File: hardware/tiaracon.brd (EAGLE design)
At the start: 50 x 50 mm, 21 parts, among them U1 ATTINY45

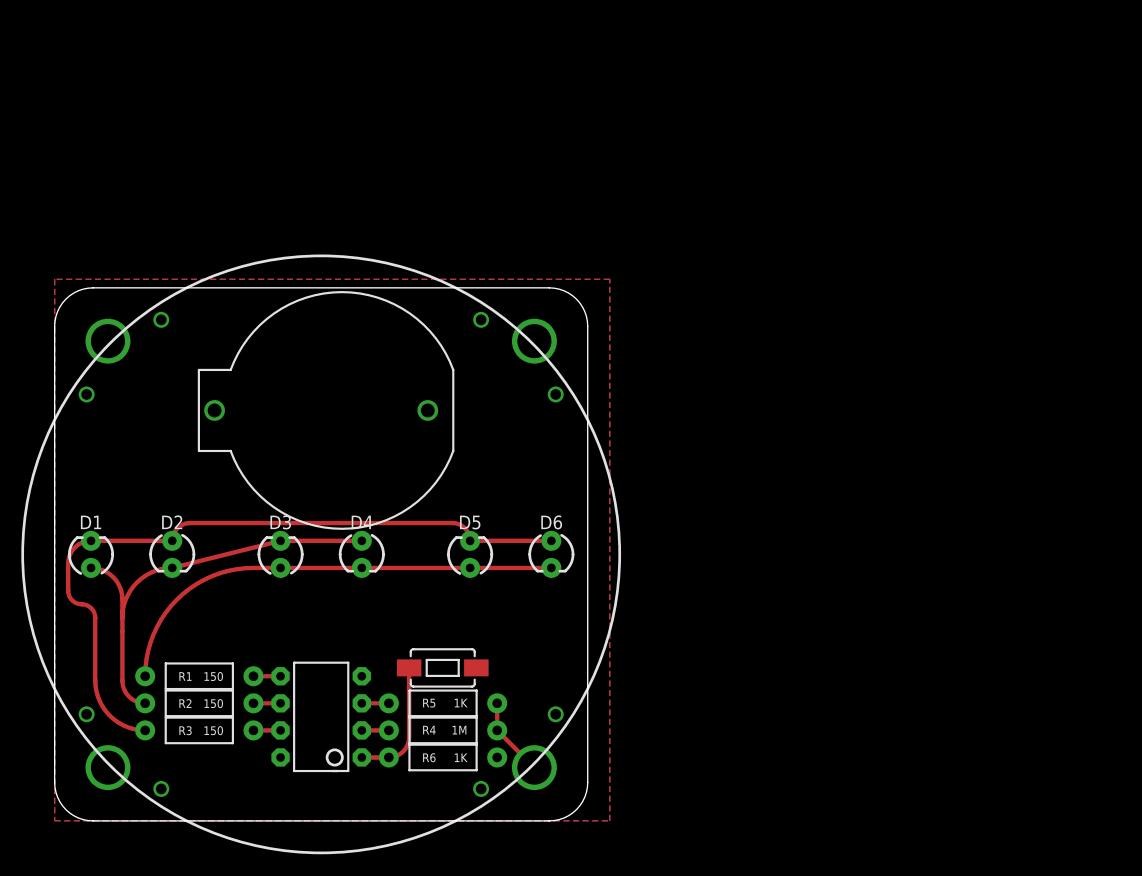
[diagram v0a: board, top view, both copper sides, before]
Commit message: adding tiara artwork, inital attempt at rough layout of components. No traces yet.
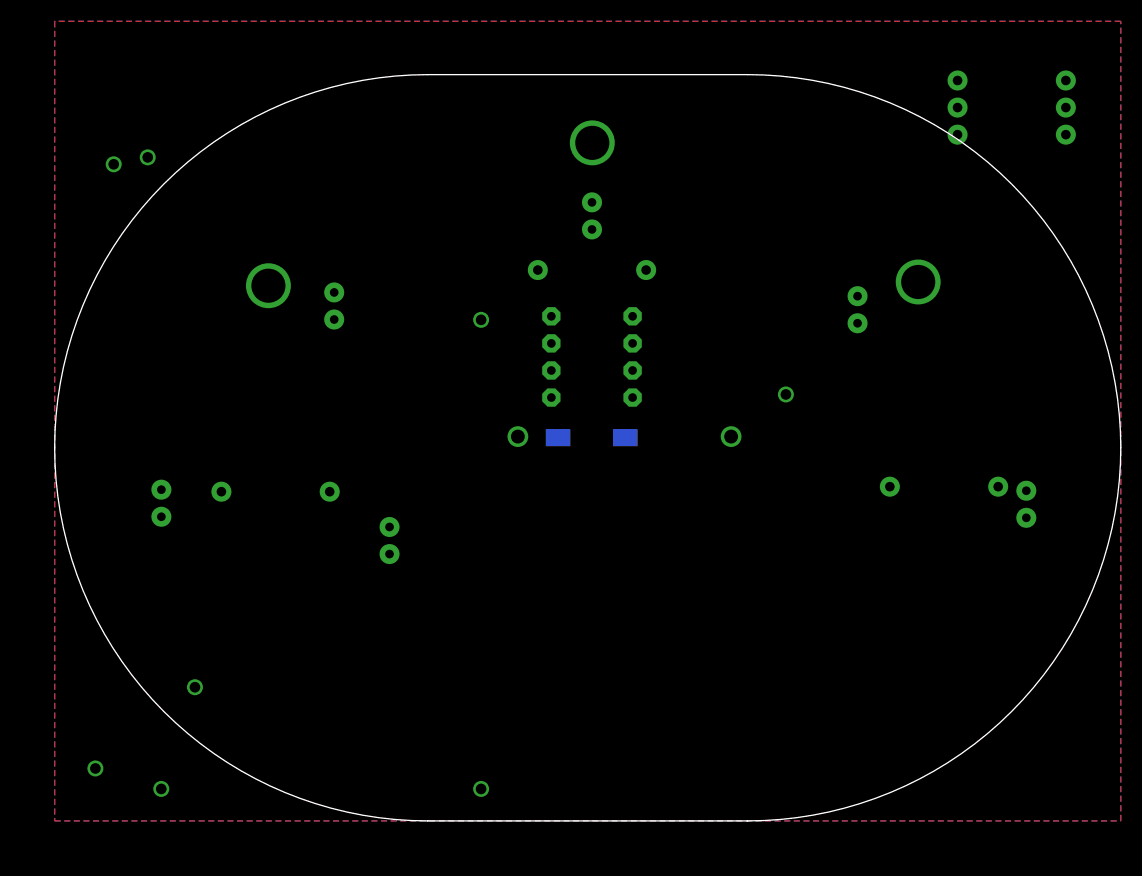
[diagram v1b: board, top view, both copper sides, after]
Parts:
- removed U$2, U$3, U$4, U$5, U$6: (no value), firefly:FIREFLY
- U$1: device securinghardware:SECURINGHARDWAREDOTCOM -> tiaracon:TIARA
- moved R4 79.1 mm to (89.8, 66.9), flipped to the bottom
- moved R5 79.1 mm to (89.8, 69.5), flipped to the bottom
- moved R6 79.1 mm to (89.8, 64.4), flipped to the bottom
- moved R2 72.7 mm to (83.4, 31.4), flipped to the bottom
- moved D4 62.5 mm to (91.1, 29.7), flipped to the bottom, turned to 90 degrees
- moved D3 58.8 mm to (75.3, 48.0), flipped to the bottom, turned to 270 degrees
- moved R3 56.8 mm to (50.4, 51.7), flipped to the bottom
- moved U$1 54.9 mm to (0.00, 0.00), flipped to the top
- moved U1 42.2 mm to (50.4, 43.5), flipped to the bottom
- moved D5 33.7 mm to (50.4, 56.8), flipped to the bottom
- moved D2 27.8 mm to (26.2, 48.3), flipped to the bottom, turned to 90 degrees
- moved S1 25.7 mm to (50.4, 35.9), flipped to the bottom
- moved BAT1 24.9 mm to (51.6, 36.0), flipped to the bottom
- moved R1 18.7 mm to (20.7, 30.9), flipped to the bottom, turned to 0 degrees
- moved D6 15.2 mm to (31.4, 26.3), flipped to the bottom, turned to 90 degrees
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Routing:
- net N$7: track 66.2 -> 0.00 mm
- net N$6: track 42.3 -> 0.00 mm
- net N$8: track 39.5 -> 0.00 mm
- net N$11: track 11.7 -> 0.00 mm
- net RING: track 7.48 -> 0.00 mm, vias 1 -> 0
- net N$5: track 2.54 -> 0.00 mm
- net N$4: track 2.54 -> 0.00 mm
- net N$3: track 2.54 -> 0.00 mm
- net N$2: track 2.54 -> 0.00 mm
- net N$1: track 2.54 -> 0.00 mm
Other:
- board size 50 x 50 mm -> 100 x 70 mm
- board text removed: "Jar of Fireflies"
- board text removed: "Jar of Fireflies V1.1 https://git.io/fireflies"
- board text removed: "Joe FitzPatrick @securelyfitz"
- board text removed: "by @securelyfitz"
- board text removed: "joefitz@securinghardware.com"

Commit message: including updated brd and sch files. changed switch to through hole, etc
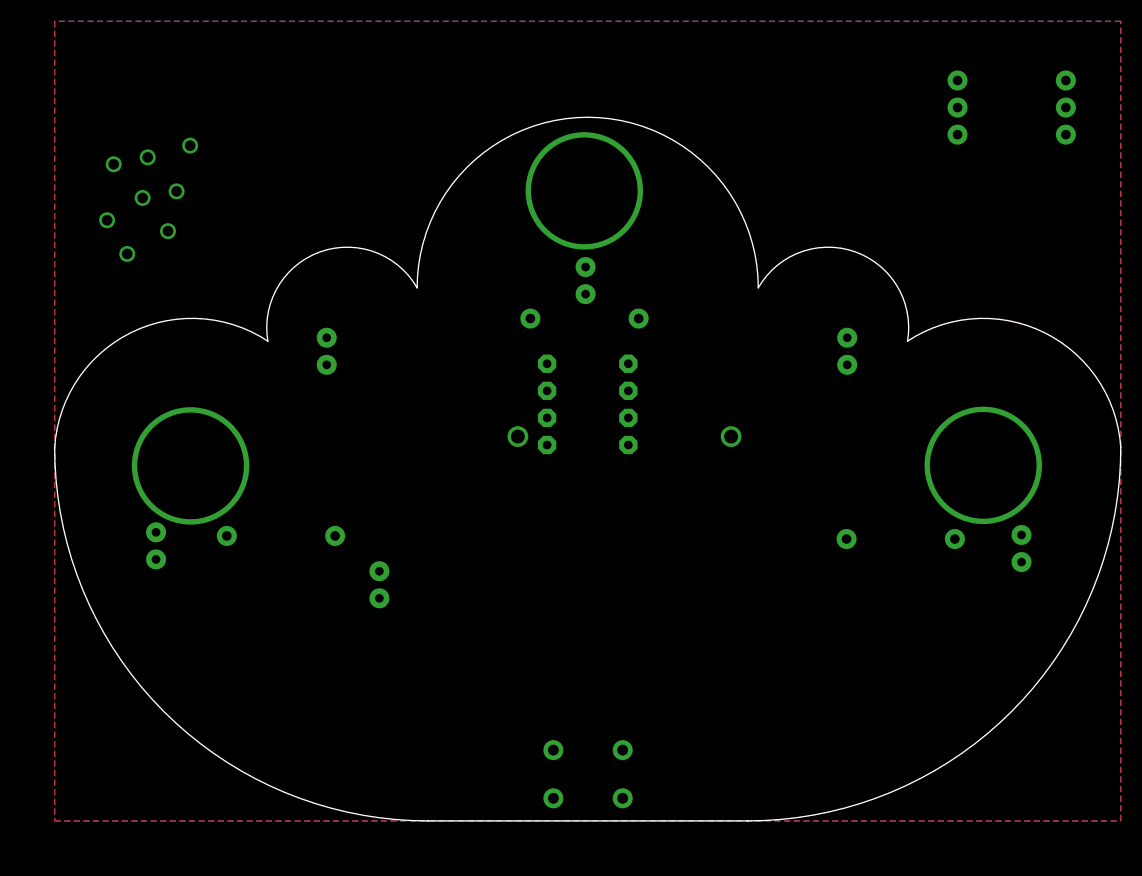
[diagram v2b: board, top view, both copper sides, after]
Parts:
- S1: value SWITCH-MOMENTARY-2SMD-1101NE -> SWITCH-MOMENTARY-2PTH; device SparkFun-Electromechanical:TACTILE-SWITCH-1101NE -> SparkFun-Electromechanical:TACTILE-PTH
- moved S1 31.6 mm to (50.0, 4.38), turned to 0 degrees
- moved R2 6.37 mm to (79.4, 26.4)
- moved D5 6.10 mm to (49.8, 50.7)
- moved R3 4.60 mm to (49.7, 47.1)
- moved U1 4.47 mm to (50.0, 39.1)
- moved D2 4.31 mm to (25.5, 44.0)
- moved D6 4.26 mm to (30.5, 22.1)
- moved R1 4.18 mm to (21.2, 26.7)
- moved D4 4.17 mm to (90.7, 25.6)
- moved D1 4.03 mm to (9.51, 25.8)
- moved D3 4.02 mm to (74.3, 44.0), turned to 90 degrees
- moved U$1 3.57 mm to (-0.70, -3.50)
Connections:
- net N$11: now also S1.3; no longer S1.2
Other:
- board size 100 x 70 mm -> 100 x 66 mm

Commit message: circuit laid out, added ponies and text. still need to adjust lanyard holes
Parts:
- removed R4: 1M, SparkFun-Passives:AXIAL-0.4
- removed R5, R6: 1K, SparkFun-Passives:AXIAL-0.4
- added U$2: (no value), tiaracon:PONY
- moved D2 25.5 mm to (49.8, 52.1), turned to 180 degrees
- moved D5 25.1 mm to (25.4, 44.6)
- moved D6 21.5 mm to (9.35, 26.0), turned to 270 degrees
- moved D1 21.2 mm to (30.5, 22.8)
- moved BAT1 16.6 mm to (50.1, 19.5), turned to 90 degrees
- moved R3 0.61 mm to (49.8, 47.7), turned to 0 degrees
- turned D3 to 270 degrees
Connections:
- removed net N$11: R6.P$2, S1.3, U1.1
- removed net N$5: R5.P$1, U1.3
- removed net RING: R4.P$2, R5.P$2
- net GND: now also S1.3; no longer S1.1
- net N$4: now also S1.1; no longer R4.P$1
- net VCC: no longer R6.P$1
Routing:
- net N$8: track 0.00 -> 175.2 mm
- net N$6: track 0.00 -> 119.7 mm
- net N$7: track 0.00 -> 96.4 mm
- net N$1: track 0.00 -> 35.9 mm
- net N$4: track 0.00 -> 35.2 mm
- net N$2: track 0.00 -> 32.2 mm
- net N$3: track 0.00 -> 11.1 mm
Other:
- board text added: "TiaraCon 2016! Artwork: ?? PCB: @securelyfitz In partnership w/ #brainbabe & CyberSN https://git.io /tiaracon"

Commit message: final round of changes, pcb to be ordered if approved...
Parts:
- moved D2 8.81 mm to (49.6, 60.9), turned to 90 degrees
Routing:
- net N$7: track 96.4 -> 103.4 mm
- net N$8: track 175.2 -> 181.7 mm
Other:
- board text added: "TiaraCon 2016! In partnership w/ #brainbabe & CyberSN Artwork: TeamTiara PCB: @securelyfitz https://git.io /tiaracon"
- board text removed: "TiaraCon 2016! Artwork: ?? PCB: @securelyfitz In partnership w/ #brainbabe & CyberSN https://git.io /tiaracon"
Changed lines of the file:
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@@
 <layer number="27" name="tValues" color="7" fill="1" visible="yes" active="yes"/>
 <layer number="28" name="bValues" color="7" fill="1" visible="yes" active="yes"/>
-<layer number="29" name="tStop" color="7" fill="3" visible="no" active="yes"/>
+<layer number="29" name="tStop" color="7" fill="3" visible="yes" active="yes"/>
 <layer number="30" name="bStop" color="7" fill="6" visible="yes" active="yes"/>
 <layer number="31" name="tCream" color="7" fill="4" visible="no" active="yes"/>
@@
 <wire x1="35" y1="0" x2="0" y2="35" width="0" layer="20" curve="-90"/>
 <wire x1="34" y1="50" x2="66" y2="50" width="0" layer="20" curve="-180"/>
-<text x="73.66" y="13.97" size="1.6764" layer="52" font="vector" rot="MR0" align="center">TiaraCon 2016!
-Artwork: ??
+<text x="76.5" y="14.5" size="1.6764" layer="52" font="vector" rot="MR0" align="center">TiaraCon 2016!
+In partnership w/
+#brainbabe &amp; CyberSN
+Artwork: TeamTiara
 PCB: @securelyfitz
-In partnership w/
-#brainbabe
-  &amp; CyberSN
 https://git.io
   /tiaracon</text>
@@
 <attribute name="VALUE" x="28.869" y="24.685" size="1.27" layer="28" ratio="10" rot="MR90"/>
 </element>
-<element name="D2" library="SparkFun-LED" package="LED3MM" value="" x="49.75" y="52.09" smashed="yes" rot="MR180">
-<attribute name="NAME" x="46.75" y="53.195" size="1.27" layer="26" ratio="10" rot="MR270" align="center-left"/>
-<attribute name="VALUE" x="51.655" y="53.741" size="1.27" layer="28" ratio="10" rot="MR180"/>
+<element name="D2" library="SparkFun-LED" package="LED3MM" value="" x="49.62" y="60.9" smashed="yes" rot="MR90">
+<attribute name="NAME" x="48.515" y="57.9" size="1.27" layer="26" ratio="10" rot="MR180" align="center-left"/>
+<attribute name="VALUE" x="47.969" y="62.805" size="1.27" layer="28" ratio="10" rot="MR90"/>
 </element>
 <element name="D5" library="SparkFun-LED" package="LED3MM" value="" x="25.41" y="44.6" smashed="yes" rot="MR90">
@@
 <wire x1="43.41" y1="45.87" x2="44.67" y2="47.73" width="0.4064" layer="16"/>
 <wire x1="44.67" y1="47.73" x2="44.62" y2="48.23" width="0.4064" layer="16"/>
-<wire x1="44.62" y1="48.23" x2="48.48" y2="52.09" width="0.4064" layer="16"/>
+<wire x1="44.62" y1="48.23" x2="49.62" y2="59.63" width="0.4064" layer="16"/>
 </signal>
 <signal name="VCC">
@@
 <wire x1="64.2" y1="3.9" x2="84.44" y2="24.14" width="0.4064" layer="16"/>
 <wire x1="84.44" y1="24.14" x2="84.44" y2="26.44" width="0.4064" layer="16"/>
-<wire x1="51.02" y1="52.09" x2="58.4" y2="52.09" width="0.4064" layer="16"/>
+<wire x1="49.62" y1="62.17" x2="49.68" y2="62.23" width="0.4064" layer="16"/>
+<wire x1="49.68" y1="62.23" x2="50.8" y2="62.23" width="0.4064" layer="16"/>
+<wire x1="50.8" y1="62.23" x2="58.4" y2="52.09" width="0.4064" layer="16"/>
 <wire x1="58.4" y1="52.09" x2="62.23" y2="48.26" width="0.4064" layer="16"/>
 <wire x1="80.01" y1="41.91" x2="93.98" y2="41.91" width="0.4064" layer="16"/>
@@
 <wire x1="73.66" y1="48.26" x2="80.01" y2="41.91" width="0.4064" layer="16"/>
 </signal>
-<signal name="N$12">
-<via x="49.68" y="59.1" extent="1-16" drill="10"/>
-</signal>
 <signal name="N$4">
